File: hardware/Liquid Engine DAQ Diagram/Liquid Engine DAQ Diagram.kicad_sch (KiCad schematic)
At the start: 48 parts, among them CN10 Conn_02x17_Odd_Even, CN7 Conn_02x10_Odd_Even, CN8 Conn_02x08_Odd_Even, CN9 Conn_02x15_Odd_Even, J1 Conn_01x14_Pin, J10 Conn_01x14_Pin, J11 Conn_01x09_Pin, J12 Conn_01x02_Pin, J13 Conn_01x06_Pin, J14 Conn_01x06_Pin, J15 Conn_01x04_Pin, J16 Conn_01x04_Pin, J17 Conn_01x03_Pin, J18 Conn_01x03_Pin, J19 Conn_01x03_Pin, J2 Conn_01x14_Pin, J20 Conn_01x03_Pin, J21 Conn_01x03_Pin, J22 Conn_01x03_Pin, J23 Conn_01x03_Pin, J24 Conn_01x03_Pin, J25 Conn_01x16_Pin, J26 Conn_01x06_Pin, J27 Conn_01x06_Pin, J28 Conn_01x02_Pin, J29 Conn_01x02_Pin, J3 Conn_01x05_Pin, J30 Conn_01x02_Pin, J31 Conn_01x02_Pin, J32 Conn_01x06_Pin, J33 Conn_01x06_Pin, J36 Conn_01x02_Pin, J37 Conn_01x04_Pin, J38 Conn_01x06_Pin, J39 Conn_01x06_Pin, J4 Conn_01x08_Pin, J40 Conn_01x08_Pin, J41 Conn_01x08_Pin, J42 Conn_01x02_Pin, J43 Conn_01x04_Pin, J44 CN11, J5 Conn_01x08_Pin, J6 DIN41612_02x08_AB_EvenPins, J7 Conn_01x14_Pin, J8 Conn_01x08_Pin, J9 Conn_01x05_Pin

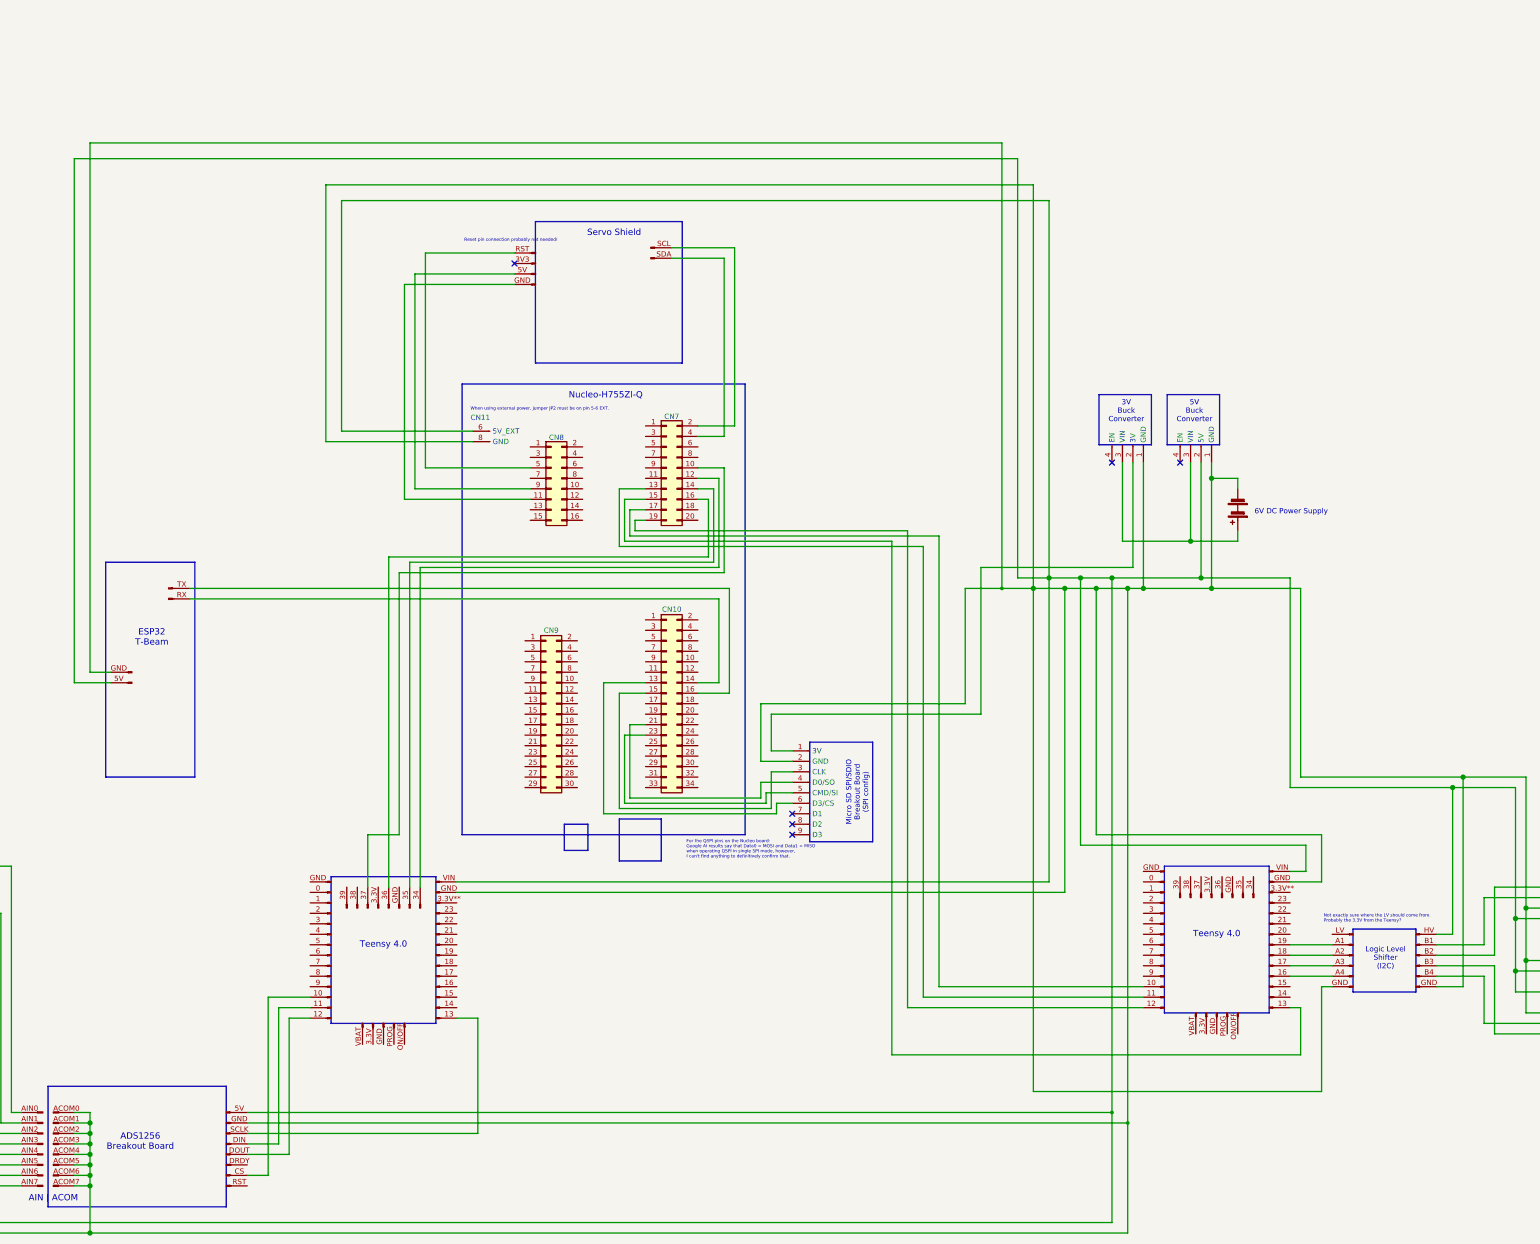
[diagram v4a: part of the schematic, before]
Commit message: updated wiring diagram and switched back to Arduino IDE for code
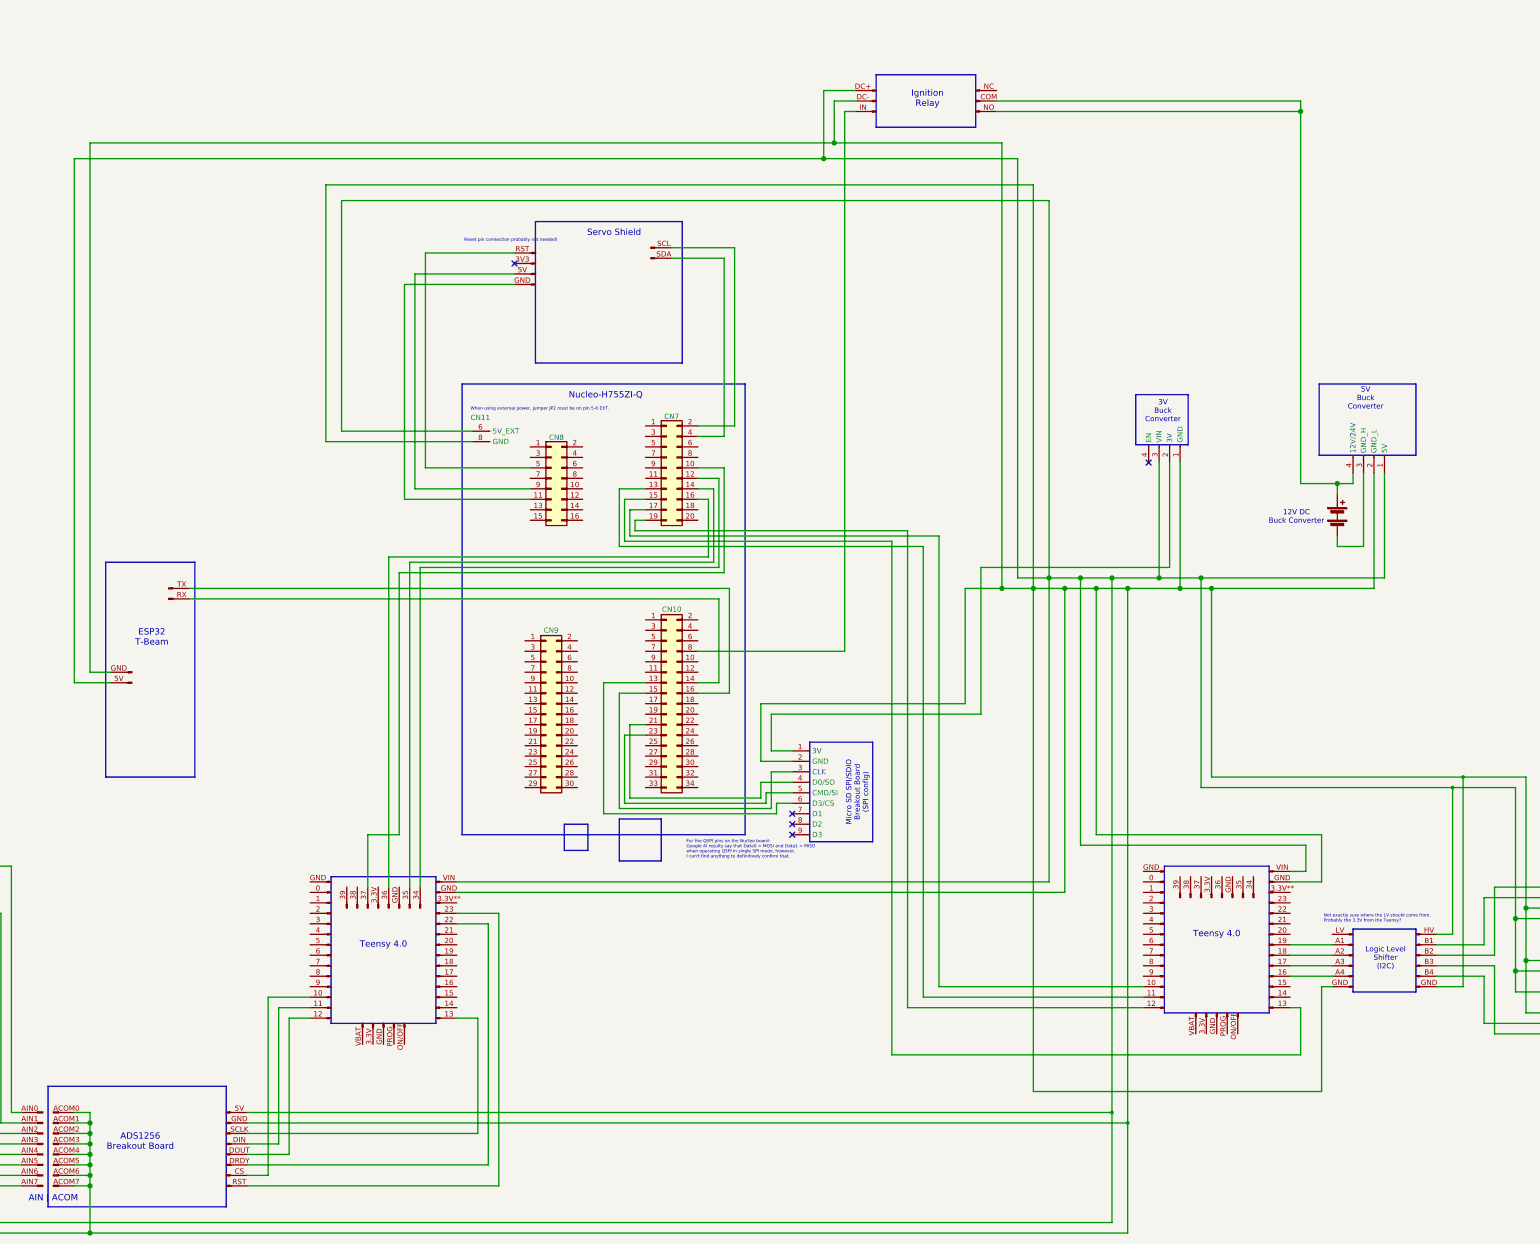
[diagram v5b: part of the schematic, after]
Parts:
- removed J15: Conn_01x04_Pin, symbol Connector:Conn_01x04_Pin
- added J34, J35: Conn_01x03_Pin, symbol Connector:Conn_01x03_Pin
- added J45: Conn_01x04_Pin, symbol Connector:Conn_01x04_Pin
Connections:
- net at J1.VIN, J10.VIN, J14.1 (VCC)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: now also J37.3 (VIN), J35.DC+, J45.1 (5V)
- net at J1.GND, J10.GND, J11.2 (GND)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: now also J35.DC-, J45.2 (GND_L); no longer BT2.2 (-)
- net at BT2.1 (+): now also J34.COM, J34.NO, J45.4 (12V/24V); no longer J37.3 (VIN)
- net at J5.DRDY: now also J1.22
- net at J5.RST: now also J1.23
- net at CN10.8 (Pin_8): now also J35.IN
- new net: BT2.2 (-), J45.3 (GND_H)
- no-connect marks 15 -> 14
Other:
- note added: "12V DC Buck Converter"
- note added: "Ignition Relay"
- note removed: "6V DC Power Supply"
